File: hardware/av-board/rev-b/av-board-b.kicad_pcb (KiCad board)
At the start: 4 copper layers, 94.6 x 69.4 mm, 176 parts, among them J1 RCA Y, J10 2x20 socket, J2 RCA Pb, J3 RCA Pr, J4 RCA L, J5 RCA R, J6 HDMI-001, J9 2x20 socket, SW1 TS-1187A-B-A-B, SW2 TS-1187A-B-A-B, U1 ADV7181DBCPZ-RL, U10 TPD4E05U06DQAR, U2 ADV7511KSTZ, U3 PCM1808PWR, U4 TLV62569DBVR, U5 TPS7A7001DDAR, U6 TPS7A7001DDAR, U7 TPS7A7001DDAR, U8 TPD4E05U06DQAR, U9 TPD4E05U06DQAR, Y1 28.63636MHz 20pF

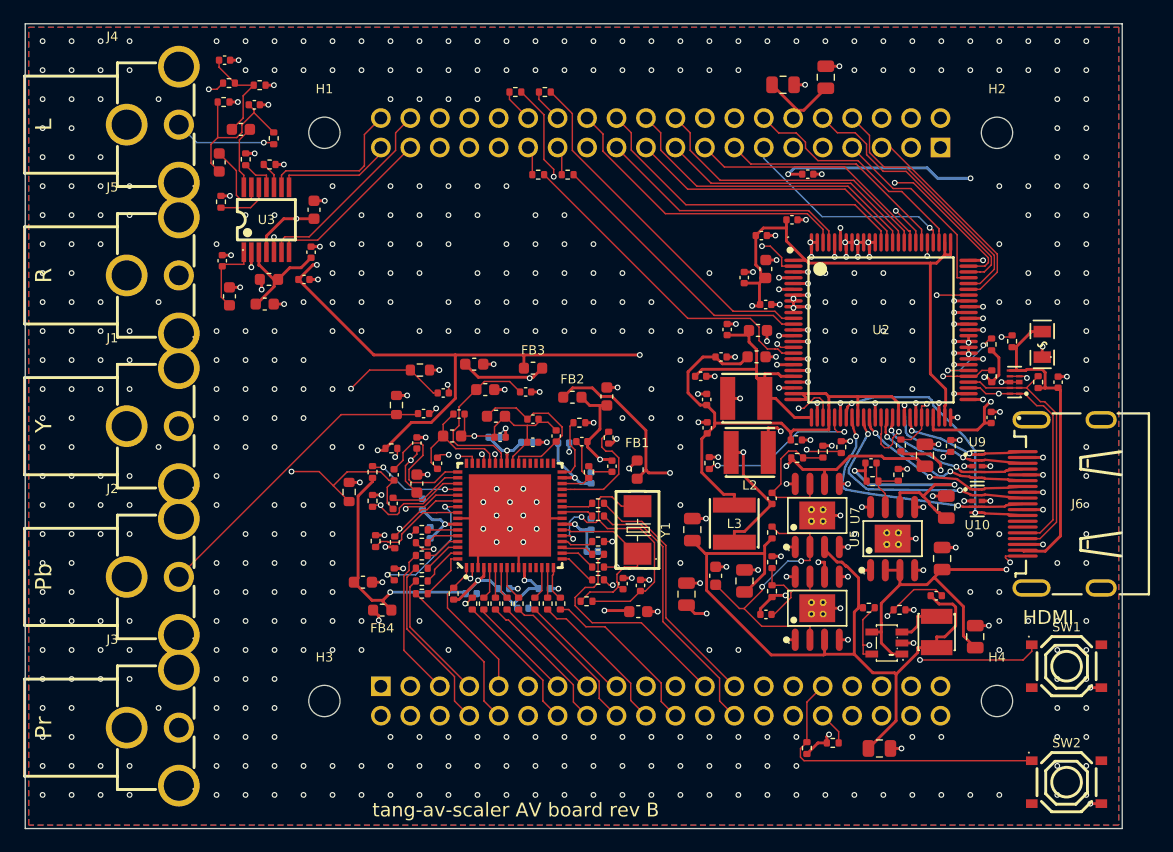
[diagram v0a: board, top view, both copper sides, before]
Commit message: Rev B: SMT on the top only, resistor arrays, a BOM without the RCA jacks
Every SMT part is now on the top (only the through-hole J9/J10 sockets sit underneath), so
JLCPCB assembles one side. To make room for the ADV7181D decoupling on the top, the three
runs of four pixel pins get 4 x 0402 33 R arrays at the pins own 0.5 mm pitch, in line with
them (163 parts, from 172); the band between the chip and its resistors is kept for the lines
and each supply pin 100 nF is placed first (2.7-4.3 mm from its pin).

gen_fab.py writes a BOM + CPL per assembly variant (VARIANTS in board.py); rev B hand-jacks
leaves J1-J5 for soldering by hand. Same Gerbers.

The routing flow does the hand steps now: a post_route hook (rev B: the TMDS pairs ripped up
and laid pair-wise on the outer layers), then finish_unconnected (DRC unconnected list ->
copper islands -> nearest pad pair -> mazeroute.py). mazeroute keeps 10 um of slack over the
clearance and its new vias clear of its own nets drills. snap.py frames on the outline.

DRC: no errors, no unconnected items. ERC clean, schematic = board.py.

Co-Authored-By: Claude Opus 5.5 <noreply@anthropic.com>
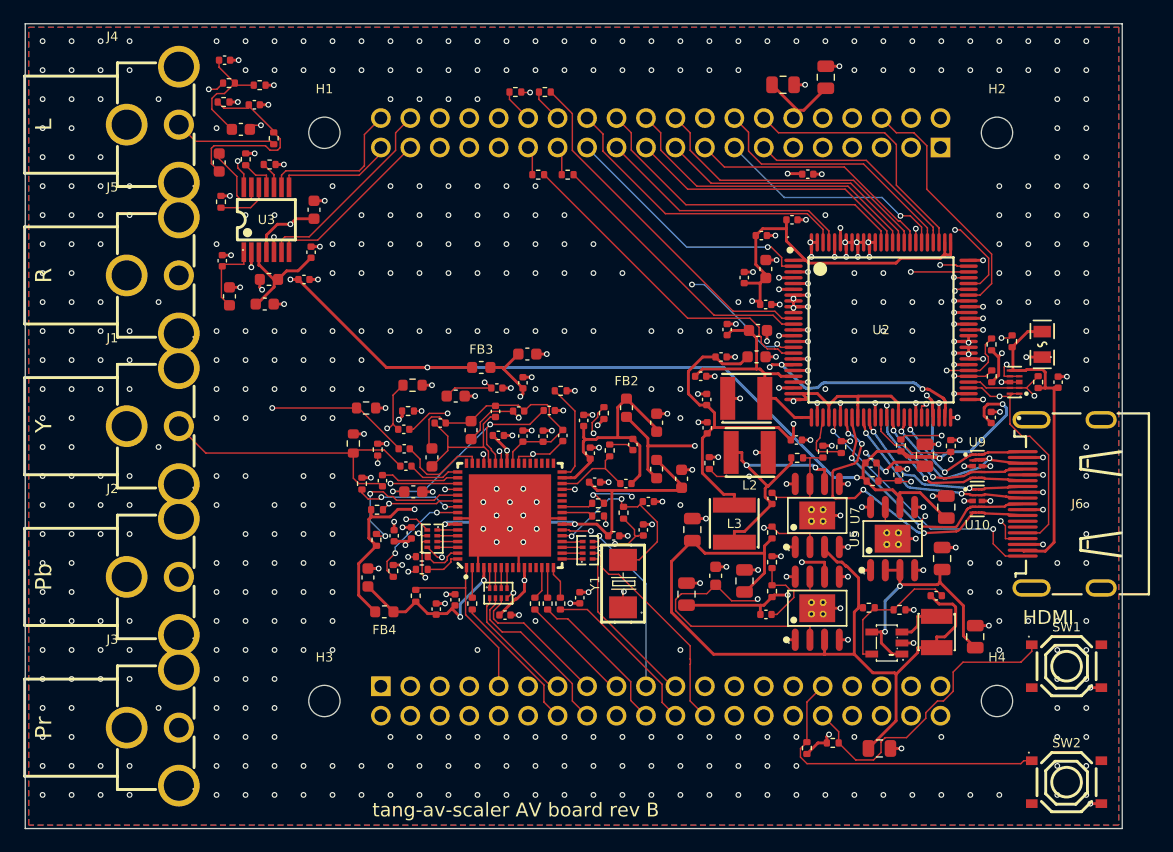
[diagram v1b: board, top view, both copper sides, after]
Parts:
- removed R53, R54, R55, R56: 49.9, Resistor_SMD:R_0402_1005Metric
- removed R57: 887, Resistor_SMD:R_0402_1005Metric
- removed R58, R59, R60, R61, R62, R63: 2k, Resistor_SMD:R_0402_1005Metric
- removed R64: 10k, Resistor_SMD:R_0402_1005Metric
- added RN1: 33, lcsc:RES-ARRAY-SMD_0402-8P-L2.0-W1.0-BL, F.Cu at (109.3, 65.0)
- added RN2: 33, lcsc:RES-ARRAY-SMD_0402-8P-L2.0-W1.0-BL, F.Cu at (115.0, 69.7)
- added RN3: 33, lcsc:RES-ARRAY-SMD_0402-8P-L2.0-W1.0-BL, F.Cu at (122.7, 66.0)
- C44, C45, C46, C47, C48, C49, C50, C51, C52, C53, C54, C55: moved to F.Cu
- R25, R26, R27, R28, R29, R30: value 33 -> 4.7k
- R31, R32, R33, R34, R35, R36: value 33 -> 10k
- R37, R38, R39, R40: value 4.7k -> 10k
- R41, R42: value 4.7k -> 49.9
- R43, R44: value 10k -> 49.9
- R45: value 10k -> 887
- R46, R47, R48, R49, R50, R51: value 10k -> 2k
- moved R51 74.4 mm to (161.6, 51.5), turned to 90 degrees
- moved R50 71.1 mm to (159.3, 48.0), turned to 90 degrees
- moved R47 66.3 mm to (157.5, 48.2)
- moved R46 64.9 mm to (157.6, 51.0), turned to 90 degrees
- moved R49 64.1 mm to (154.0, 57.0)
- moved R48 62.3 mm to (149.7, 57.0)
- moved R52 50.7 mm to (133.2, 58.5), turned to 90 degrees
- moved R40 46.9 mm to (94.4, 25.9), turned to 0 degrees
- moved R34 41.7 mm to (95.3, 32.7), turned to 0 degrees
- moved R35 40.4 mm to (93.2, 32.3), turned to 90 degrees
- moved R45 40.1 mm to (144.6, 57.1)
- moved R39 38.1 mm to (91.8, 25.7), turned to 0 degrees
- moved R36 37.0 mm to (91.1, 36.0), turned to 90 degrees
- moved R37 36.4 mm to (95.6, 30.5)
- moved R41 36.0 mm to (119.0, 26.5), turned to 0 degrees
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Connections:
- R17 pad 1: AV_Y7 -> AV_C7
- R17 pad 2: IN_Y7 -> IN_C7
- R18 pad 1: AV_Y6 -> AV_C6
- R18 pad 2: IN_Y6 -> IN_C6
- R19 pad 1: AV_Y5 -> AV_C5
- R19 pad 2: IN_Y5 -> IN_C5
- R20 pad 1: AV_Y4 -> AV_C1
- R20 pad 2: IN_Y4 -> IN_C1
- R21 pad 1: AV_Y3 -> AV_C0
- R21 pad 2: IN_Y3 -> IN_C0
- R22 pad 1: AV_Y2 -> AV_HS
- R22 pad 2: IN_Y2 -> IN_HS
- R23 pad 1: AV_Y1 -> AV_VS
- R23 pad 2: IN_Y1 -> IN_VS
- R24 pad 1: AV_Y0 -> AV_DE
- R24 pad 2: IN_Y0 -> IN_DE
- R25 pad 1: AV_C7 -> 3V3
- R25 pad 2: IN_C7 -> IN_SCL
- R26 pad 1: AV_C6 -> 3V3
- R26 pad 2: IN_C6 -> IN_SDA
- R27 pad 1: AV_C5 -> IN_RESET_N
- R27 pad 2: IN_C5 -> GND
- R28 pad 1: AV_C4 -> AV_DVDDIO
- R28 pad 2: IN_C4 -> IN_INT
- R29 pad 1: AV_C3 -> AV_DVDDIO
- R29 pad 2: IN_C3 -> ALSB
- R30 pad 1: AV_C2 -> AV_DVDDIO
- R30 pad 2: IN_C2 -> PWRDWN
- R31 pad 1: AV_C1 -> PD_FB
- R31 pad 2: IN_C1 -> GND
- R32 pad 1: AV_C0 -> PD_HS_IN_CS_IN
- R32 pad 2: IN_C0 -> GND
- R33 pad 1: AV_LLC -> PD_VS_IN
- R33 pad 2: IN_LLC -> GND
- R34 pad 1: AV_HS -> MD0
- R34 pad 2: IN_HS -> GND
- R35 pad 1: AV_VS -> MD1
- R35 pad 2: IN_VS -> GND
- R36 pad 1: AV_DE -> FMT
- R36 pad 2: IN_DE -> GND
- R37 pad 1: 3V3 -> RCA_L
- R37 pad 2: IN_SCL -> AUD_DIV_L
- R38 pad 1: 3V3 -> AUD_DIV_L
- R38 pad 2: IN_SDA -> GND
- R39 pad 1: IN_RESET_N -> RCA_R
- R39 pad 2: GND -> AUD_DIV_R
- R40 pad 1: AV_DVDDIO -> AUD_DIV_R
- R40 pad 2: IN_INT -> GND
- R41 pad 1: AV_DVDDIO -> OUT_MCLK
- R41 pad 2: ALSB -> TX_MCLK
- R42 pad 1: AV_DVDDIO -> OUT_SCLK
- R42 pad 2: PWRDWN -> TX_SCLK
- R43 pad 1: PD_FB -> OUT_LRCLK
- R43 pad 2: GND -> TX_LRCLK
- R44 pad 1: PD_HS_IN_CS_IN -> OUT_I2S0
- R44 pad 2: GND -> TX_I2S0
- R45 pad 1: PD_VS_IN -> R_EXT
- R46 pad 1: MD0 -> 3V3
- R46 pad 2: GND -> OUT_SCL
- R47 pad 1: MD1 -> 3V3
- R47 pad 2: GND -> OUT_SDA
- R48 pad 1: FMT -> 3V3
- R48 pad 2: GND -> OUT_INT
- R49 pad 1: RCA_L -> OUT_PD
- R49 pad 2: AUD_DIV_L -> GND
- R50 pad 1: AUD_DIV_L -> HDMI_5V
- R50 pad 2: GND -> HDMI_SCL
- R51 pad 1: RCA_R -> HDMI_5V
- R51 pad 2: AUD_DIV_R -> HDMI_SDA
- R52 pad 1: AUD_DIV_R -> HDMI_HPD
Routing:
- net AV_DVDD: track 51.5 -> 38.6 mm, vias 4 -> 3
- net AV_DVDDIO: track 53.6 -> 65.7 mm, vias 4 -> 6
- net EN_1V8: track 24.2 -> 34.3 mm
- net XTAL1: track 26.3 -> 16.5 mm
- net +5V: track 194.8 -> 186.1 mm
- net IN_Y0: track 13.1 -> 21.3 mm, vias 0 -> 1
- net AIN_Y: track 12.1 -> 4.59 mm
- net CML: track 13.2 -> 20.7 mm
- net FB_3V3: track 5.84 -> 13.0 mm, vias 0 -> 2
- net 1V8A: track 47.5 -> 40.7 mm, vias 4 -> 3
- net IN_VS: track 13.5 -> 20.0 mm, vias 0 -> 1
- net OUT_C0: track 29.3 -> 22.8 mm, vias 1 -> 0
- net RCA_PR: track 44.3 -> 38.3 mm
- net 2V5: track 66.7 -> 72.6 mm
- net R_EXT: track 11.0 -> 5.15 mm, vias 2 -> 0
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
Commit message: Rev B reviewed against every data sheet; supplies, stack-up and TMDS fixed
review.md: each part against its document, for margin, not just limits. Fixed:
- Supply sequencing: the ADV7181D allows 3.3 V at most 2 V above and 0.3 V below the 1.8 V
  rails [DS Table 5]; rev A RC enable put 3V3 30 ms ahead. Now buck -> 3V6 -> 3V3 LDO ->
  1.8 V LDOs fed and enabled by 3V3, plus a B5819W clamp 1V8A -> 3V3 for power-down. The 3V3
  LDO runs from 3.6 V (0.17 W, was 0.94 W).
- Ferrites: the 0.2 A / 0.45 R beads dropped AVDD under 3.15 V at the LDO low limit;
  BLM18PG121SN1D (2 A, 50 mR), a basic part.
- Crystal: YXC X50322863636MSB2GI (476 in stock, +-10 ppm) for the 68-in-stock TXM.
- Stack-up: In2 a second ground plane, signals on F/B only, each over its own plane (B.Cu had
  no plane closer than 1.3 mm) [HWG 7.2].
- TMDS: the pairs are laid by the generator on F.Cu, 0.25/0.25 mm at the pins 0.5 mm pitch
  (103 R), coupled pin to connector, no vias, 0.83 mm intra-pair skew; a corridor kept free;
  the pins between the pairs escape inwards under the package.
- R_EXT 2.2 mm from its pin; video inputs get a TPD4E05U06.

pcbkit: INNER_GND, ROUTE_LAYERS, MIN_VIA, TMDS geometry per revision, via sizes, pad-level
fanout skips; session() restores locked vias sizes (KiCad import resets them).

DRC: no errors, no unconnected items. ERC clean, schematic = board.py. Rev A unchanged.

Co-Authored-By: Claude Opus 5.5 <noreply@anthropic.com>
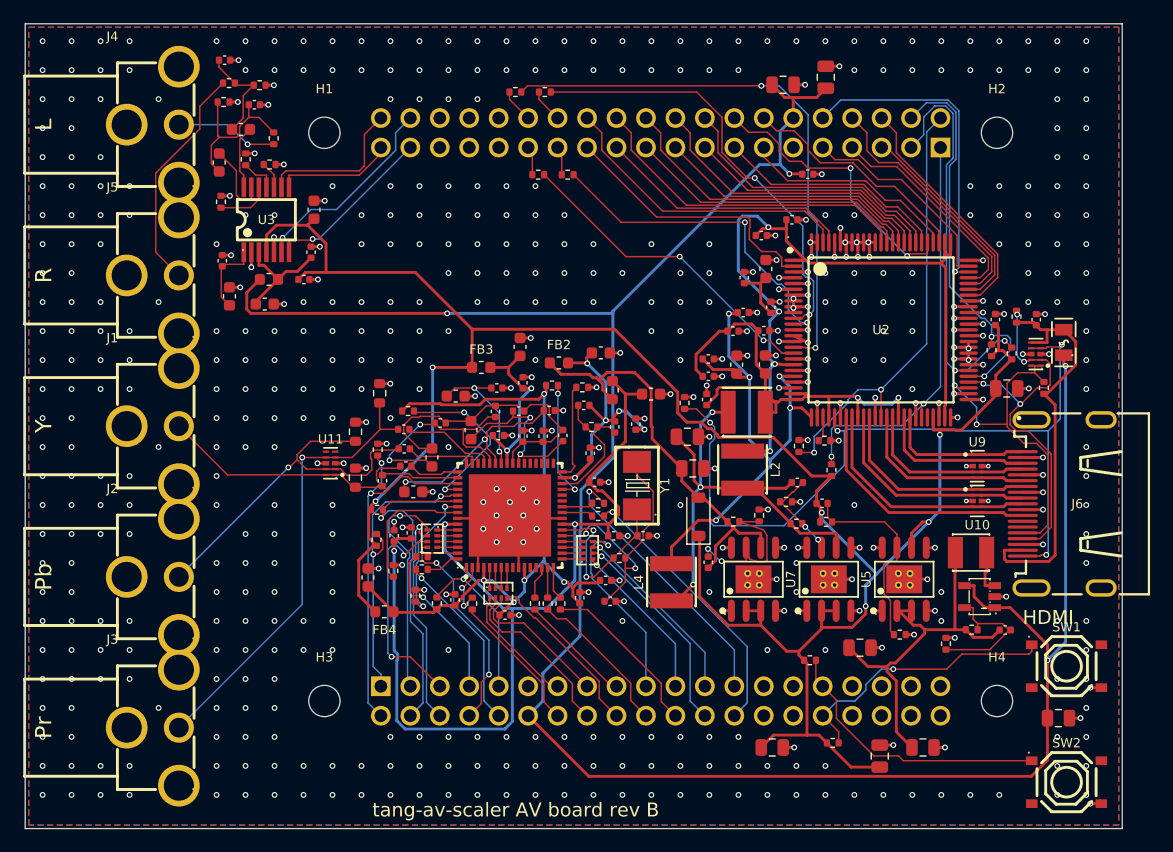
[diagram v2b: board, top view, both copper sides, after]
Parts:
- removed C77: 100n, Capacitor_SMD:C_0402_1005Metric
- removed R52: 10k, Resistor_SMD:R_0402_1005Metric
- added D1: B5819W, Diode_SMD:D_SOD-123, F.Cu at (132.3, 63.1)
- added U11: TPD4E05U06DQAR, lcsc:USON-10_L2.5-W1.0-P0.50-BL, F.Cu at (100.5, 58.5)
- C10: value 470n -> 10u; footprint Capacitor_SMD:C_0603_1608Metric -> Capacitor_SMD:C_0805_2012Metric
- C12, C15: value 10u -> 220p; footprint Capacitor_SMD:C_0805_2012Metric -> Capacitor_SMD:C_0402_1005Metric
- C13: value 220p -> 10u; footprint Capacitor_SMD:C_0402_1005Metric -> Capacitor_SMD:C_0805_2012Metric
- C16: value 220p -> 10u; footprint Capacitor_SMD:C_0402_1005Metric -> Capacitor_SMD:C_0603_1608Metric
- C23, C32, C35, C38, C40, C57, C59: value 10u -> 100n; footprint Capacitor_SMD:C_0603_1608Metric -> Capacitor_SMD:C_0402_1005Metric
- C26: value 100n -> 1n
- C27: value 1n -> 33p
- C29: value 33p -> 100n
- C31, C39, C56, C58, C60: value 100n -> 10u; footprint Capacitor_SMD:C_0402_1005Metric -> Capacitor_SMD:C_0603_1608Metric
- C33, C36, C44, C46, C48, C50, C52, C54: value 100n -> 10n
- C34, C37: value 10n -> 10u; footprint Capacitor_SMD:C_0402_1005Metric -> Capacitor_SMD:C_0603_1608Metric
- C41: value 100n -> 82n
- C42: value 82n -> 10n
- C43, C45, C47, C49, C51, C53, C55: value 10n -> 100n
- C6: value 220p -> 6.8p
- C61: value 10u -> 220p; footprint Capacitor_SMD:C_0603_1608Metric -> Capacitor_SMD:C_0402_1005Metric
- C62, C64: value 220p -> 1u; footprint Capacitor_SMD:C_0402_1005Metric -> Capacitor_SMD:C_0603_1608Metric
- C63: value 1u -> 220p; footprint Capacitor_SMD:C_0603_1608Metric -> Capacitor_SMD:C_0402_1005Metric
- C65: value 1u -> 100n; footprint Capacitor_SMD:C_0603_1608Metric -> Capacitor_SMD:C_0402_1005Metric
- C7: value 4.7u -> 10u
- C9: value 6.8p -> 220p
- FB1, FB2, FB3, FB4, FB5: value 600R -> 120R
- R10, R8: value 78.7k -> 30.1k
- R11: value 30.1k -> 75; footprint Resistor_SMD:R_0402_1005Metric -> Resistor_SMD:R_0603_1608Metric
- R14: value 75 -> 1M; footprint Resistor_SMD:R_0603_1608Metric -> Resistor_SMD:R_0402_1005Metric
- R15: value 1M -> 1.69k
- R16: value 1.69k -> 33
- R24: value 33 -> 4.7k
- R3: value 169k -> 499k
- R30: value 4.7k -> 10k
- R4: value 30.1k -> 100k
- R40: value 10k -> 49.9
- R44: value 49.9 -> 887
- R45: value 887 -> 2k
- R5: value 316k -> 169k
- R51: value 2k -> 10k
- R6: value 100k -> 30.1k
- R7: value 100k -> 78.7k
- R9: value 30.1k -> 78.7k
- moved C65 45.8 mm to (137.7, 38.9)
- moved C20 43.4 mm to (138.1, 41.7)
- moved R11 40.4 mm to (102.7, 59.7)
- moved C23 32.5 mm to (107.0, 58.7)
- moved R44 31.9 mm to (143.1, 56.5)
- moved R51 30.5 mm to (131.1, 53.3)
- moved C11 29.0 mm to (131.8, 58.9)
- moved R33 28.6 mm to (95.3, 32.7), turned to 0 degrees
- moved C8 28.1 mm to (158.8, 52.1), turned to 0 degrees
- moved C55 28.0 mm to (91.2, 41.0)
- moved C75 25.9 mm to (157.9, 46.1), turned to 90 degrees
- moved R40 24.6 mm to (119.0, 26.5)
- moved C19 23.7 mm to (103.8, 68.3), turned to 90 degrees
- moved R14 23.2 mm to (125.4, 66.7)
- moved C27 23.0 mm to (127.5, 64.8), turned to 0 degrees
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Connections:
- net SW_2V5 renamed SW_3V6
- C10 pad 1: EN_1V8 -> 3V3
- C11 pad 1: 2V5 -> 1V8A
- C12 pad 2: GND -> FB_1V8A
- C13 pad 1: 1V8A -> 3V3
- C13 pad 2: FB_1V8A -> GND
- C14 pad 1: 2V5 -> 1V8B
- C15 pad 2: GND -> FB_1V8B
- C16 pad 1: 1V8B -> AV_DVDD
- C16 pad 2: FB_1V8B -> GND
- C17 pad 1: AV_DVDD -> AV_PVDD
- C18 pad 1: AV_PVDD -> AV_AVDD
- C19 pad 1: AV_AVDD -> AV_DVDDIO
- C20 pad 1: AV_DVDDIO -> TX_DVDD
- C21 pad 1: TX_DVDD -> TX_AVDD
- C22 pad 1: TX_AVDD -> TX_PLVDD
- C23 pad 1: TX_PLVDD -> RCA_Y
- C23 pad 2: GND -> AIN_Y
- C24 pad 1: RCA_Y -> RCA_PB
- C24 pad 2: AIN_Y -> AIN_PB
- C25 pad 1: RCA_PB -> RCA_PR
- C25 pad 2: AIN_PB -> AIN_PR
- C26 pad 1: RCA_PR -> RCA_Y
- C26 pad 2: AIN_PR -> SYNC_Y
- C27 pad 1: RCA_Y -> XTAL
- C27 pad 2: SYNC_Y -> GND
- C28 pad 1: XTAL -> XTAL1
- C29 pad 1: XTAL1 -> CAPY2
- C31 pad 1: CAPY2 -> CAPY1
- C31 pad 2: GND -> CAPY2
- C34 pad 1: CAPY1 -> CAPC2
- C37 pad 1: CAPC2 -> REFOUT
- C37 pad 2: CAPY2 -> GND
- C39 pad 1: REFOUT -> CML
- C41 pad 1: CML -> ELPF_RC
- C41 pad 2: GND -> AV_PVDD
- C42 pad 1: ELPF_RC -> ELPF
- C43 pad 1: ELPF -> AV_DVDDIO
- C43 pad 2: AV_PVDD -> GND
- C47 pad 1: AV_DVDDIO -> AV_DVDD
- C5 pad 1: 3V3 -> 3V6
- C51 pad 1: AV_DVDD -> AV_PVDD
- C53 pad 1: AV_PVDD -> AV_AVDD
- C55 pad 1: AV_AVDD -> VREF
- C57 pad 1: VREF -> 5VA
- C59 pad 1: 5VA -> 3V3
- C6 pad 1: 3V3 -> 3V6
- C6 pad 2: FB_3V3 -> FB_3V6
- C61 pad 1: 3V3 -> AUD_DIV_L
- C62 pad 2: GND -> AUD_VINL
- C63 pad 1: AUD_DIV_L -> AUD_DIV_R
- C63 pad 2: AUD_VINL -> GND
- C64 pad 2: GND -> AUD_VINR
- C65 pad 1: AUD_DIV_R -> TX_DVDD
- C65 pad 2: AUD_VINR -> GND
- C69 pad 1: TX_DVDD -> TX_AVDD
- C7 pad 1: +5V -> 3V6
- C73 pad 1: TX_AVDD -> TX_PLVDD
- C75 pad 1: TX_PLVDD -> 3V3
- C76 pad 1: 3V3 -> HDMI_5V
- C8 pad 1: 2V5 -> 3V3
- C9 pad 1: 2V5 -> 3V3
- C9 pad 2: FB_2V5 -> FB_3V3
- L1 pad 2: 2V5 -> 3V6
- R10 pad 1: 1V8B -> FB_1V8B
- R10 pad 2: FB_1V8B -> GND
- R11 pad 1: FB_1V8B -> RCA_Y
- R12 pad 1: RCA_Y -> RCA_PB
- R13 pad 1: RCA_PB -> RCA_PR
- R14 pad 1: RCA_PR -> XTAL
- R14 pad 2: GND -> XTAL1
- R15 pad 1: XTAL -> ELPF
- R15 pad 2: XTAL1 -> ELPF_RC
- R16 pad 1: ELPF -> AV_C7
- R16 pad 2: ELPF_RC -> IN_C7
- R17 pad 1: AV_C7 -> AV_C6
- R17 pad 2: IN_C7 -> IN_C6
- R18 pad 1: AV_C6 -> AV_C5
- R18 pad 2: IN_C6 -> IN_C5
- R19 pad 1: AV_C5 -> AV_C1
- R19 pad 2: IN_C5 -> IN_C1
- R20 pad 1: AV_C1 -> AV_C0
- R20 pad 2: IN_C1 -> IN_C0
- R21 pad 1: AV_C0 -> AV_HS
- R21 pad 2: IN_C0 -> IN_HS
- R22 pad 1: AV_HS -> AV_VS
- R22 pad 2: IN_HS -> IN_VS
- R23 pad 1: AV_VS -> AV_DE
- R23 pad 2: IN_VS -> IN_DE
- R24 pad 1: AV_DE -> 3V3
- R24 pad 2: IN_DE -> IN_SCL
- R25 pad 2: IN_SCL -> IN_SDA
- R26 pad 1: 3V3 -> IN_RESET_N
- R26 pad 2: IN_SDA -> GND
- R27 pad 1: IN_RESET_N -> AV_DVDDIO
- R27 pad 2: GND -> IN_INT
- R28 pad 2: IN_INT -> ALSB
- R29 pad 2: ALSB -> PWRDWN
- R3 pad 1: 3V3 -> 3V6
- R3 pad 2: FB_3V3 -> FB_3V6
- R30 pad 1: AV_DVDDIO -> PD_FB
- R30 pad 2: PWRDWN -> GND
- R31 pad 1: PD_FB -> PD_HS_IN_CS_IN
- R32 pad 1: PD_HS_IN_CS_IN -> PD_VS_IN
- R33 pad 1: PD_VS_IN -> MD0
- R34 pad 1: MD0 -> MD1
- R35 pad 1: MD1 -> FMT
- R36 pad 1: FMT -> RCA_L
- R36 pad 2: GND -> AUD_DIV_L
- R37 pad 1: RCA_L -> AUD_DIV_L
- R37 pad 2: AUD_DIV_L -> GND
- R38 pad 1: AUD_DIV_L -> RCA_R
- R38 pad 2: GND -> AUD_DIV_R
- R39 pad 1: RCA_R -> AUD_DIV_R
- R39 pad 2: AUD_DIV_R -> GND
- R4 pad 1: FB_3V3 -> FB_3V6
- R40 pad 1: AUD_DIV_R -> OUT_MCLK
- R40 pad 2: GND -> TX_MCLK
- R41 pad 1: OUT_MCLK -> OUT_SCLK
- R41 pad 2: TX_MCLK -> TX_SCLK
- R42 pad 1: OUT_SCLK -> OUT_LRCLK
- R42 pad 2: TX_SCLK -> TX_LRCLK
- R43 pad 1: OUT_LRCLK -> OUT_I2S0
- R43 pad 2: TX_LRCLK -> TX_I2S0
- R44 pad 1: OUT_I2S0 -> R_EXT
- R44 pad 2: TX_I2S0 -> GND
- R45 pad 1: R_EXT -> 3V3
- R45 pad 2: GND -> OUT_SCL
- R46 pad 2: OUT_SCL -> OUT_SDA
- R47 pad 2: OUT_SDA -> OUT_INT
- R48 pad 1: 3V3 -> OUT_PD
- R48 pad 2: OUT_INT -> GND
- R49 pad 1: OUT_PD -> HDMI_5V
- R49 pad 2: GND -> HDMI_SCL
- R5 pad 1: 2V5 -> 3V3
- R5 pad 2: FB_2V5 -> FB_3V3
- R50 pad 2: HDMI_SCL -> HDMI_SDA
- R51 pad 1: HDMI_5V -> HDMI_HPD
- R51 pad 2: HDMI_SDA -> GND
- R6 pad 1: FB_2V5 -> FB_3V3
- R7 pad 1: 2V5 -> 1V8A
- R7 pad 2: EN_1V8 -> FB_1V8A
- R8 pad 1: 1V8A -> FB_1V8A
- R8 pad 2: FB_1V8A -> GND
- R9 pad 1: FB_1V8A -> 1V8B
- R9 pad 2: GND -> FB_1V8B
- U4 pad 5: FB_2V5 -> FB_3V6
- U5 pad 2: +5V -> 3V6
- U5 pad 3: +5V -> 3V6
- U6 pad 2: EN_1V8 -> 3V3
- U6 pad 3: 2V5 -> 3V3
- U7 pad 2: EN_1V8 -> 3V3
- U7 pad 3: 2V5 -> 3V3
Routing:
- net 2V5: track 72.6 -> 0.00 mm
- net AV_DVDD: track 38.6 -> 82.2 mm
- net 3V6: track 0.00 -> 34.6 mm
- net EN_1V8: track 34.3 -> 0.00 mm, vias 2 -> 0
- net TX_PLVDD: track 21.5 -> 44.7 mm, vias 0 -> 5
- net 3V3: track 174.6 -> 194.3 mm, vias 10 -> 6
- net +5V: track 186.1 -> 200.6 mm, vias 5 -> 4
- net TX_SCLK: track 34.7 -> 48.4 mm, vias 3 -> 2
- net HDMI_HPD: track 59.0 -> 71.6 mm
- net FB_2V5: track 12.3 -> 0.00 mm
- net FB_3V6: track 0.00 -> 12.0 mm
- net HDMI_SDA: track 24.1 -> 33.4 mm, vias 2 -> 4
- net OUT_SDA: track 28.2 -> 36.3 mm, vias 1 -> 2
- net HDMI_5V: track 27.8 -> 35.4 mm
- net XTAL1: track 16.5 -> 24.0 mm
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- added copper zone on In2.Cu, net GND
